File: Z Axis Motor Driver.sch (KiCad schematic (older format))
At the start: 36 parts

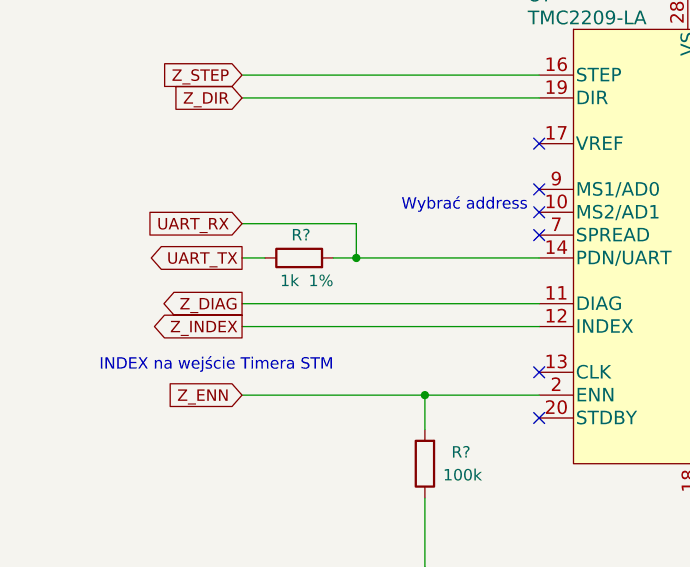
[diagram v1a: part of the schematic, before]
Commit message: Added Polyfuses and replace diodes
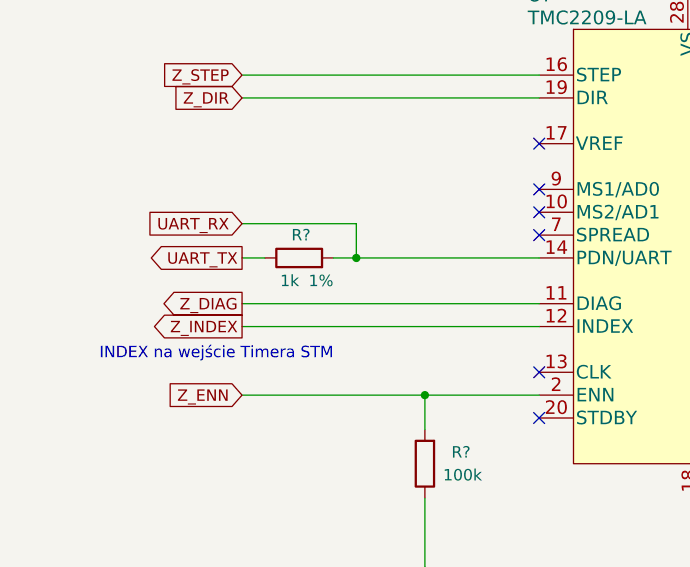
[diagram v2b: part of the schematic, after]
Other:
- note removed: "Wybrać address"
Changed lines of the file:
@@
 $Descr A4 11693 8268
 encoding utf-8
-Sheet 3 9
+Sheet 3 10
 Title "Z Axis Motor Driver"
 Date "2019-12-02"
@@
 Wire Wire Line
 	2700 3850 1400 3850
-Text Notes 1800 4150 2    50   ~ 0
+Text Notes 1800 4100 2    50   ~ 0
 INDEX na wejście Timera STM
 NoConn ~ 2700 4150
@@
 Wire Wire Line
 	2200 4700 2200 5000
-Text Notes 2650 3450 2    50   ~ 0
-Wybrać address
 Text Notes 3700 5550 2    50   ~ 0
 Pin 25 NC można podłączyć do GND jeśli poprawi to rutowanie PCB

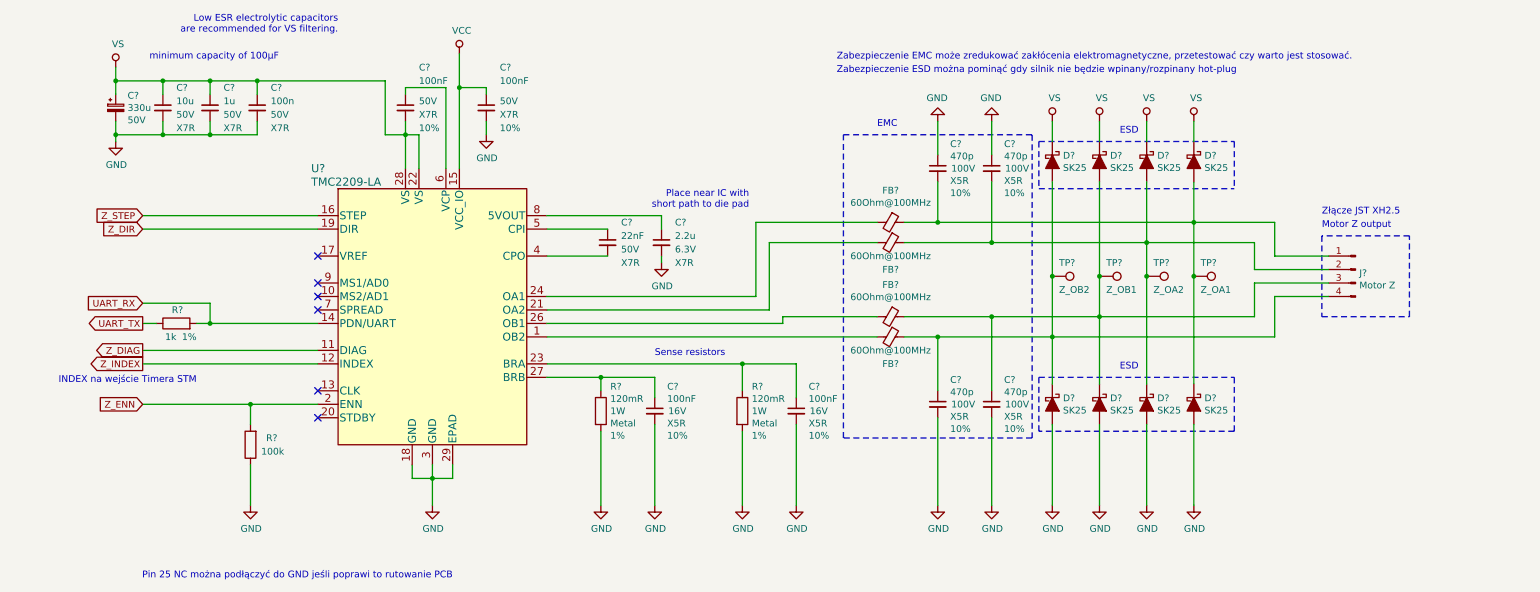
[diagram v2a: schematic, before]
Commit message: Numbering and finishing the schematic
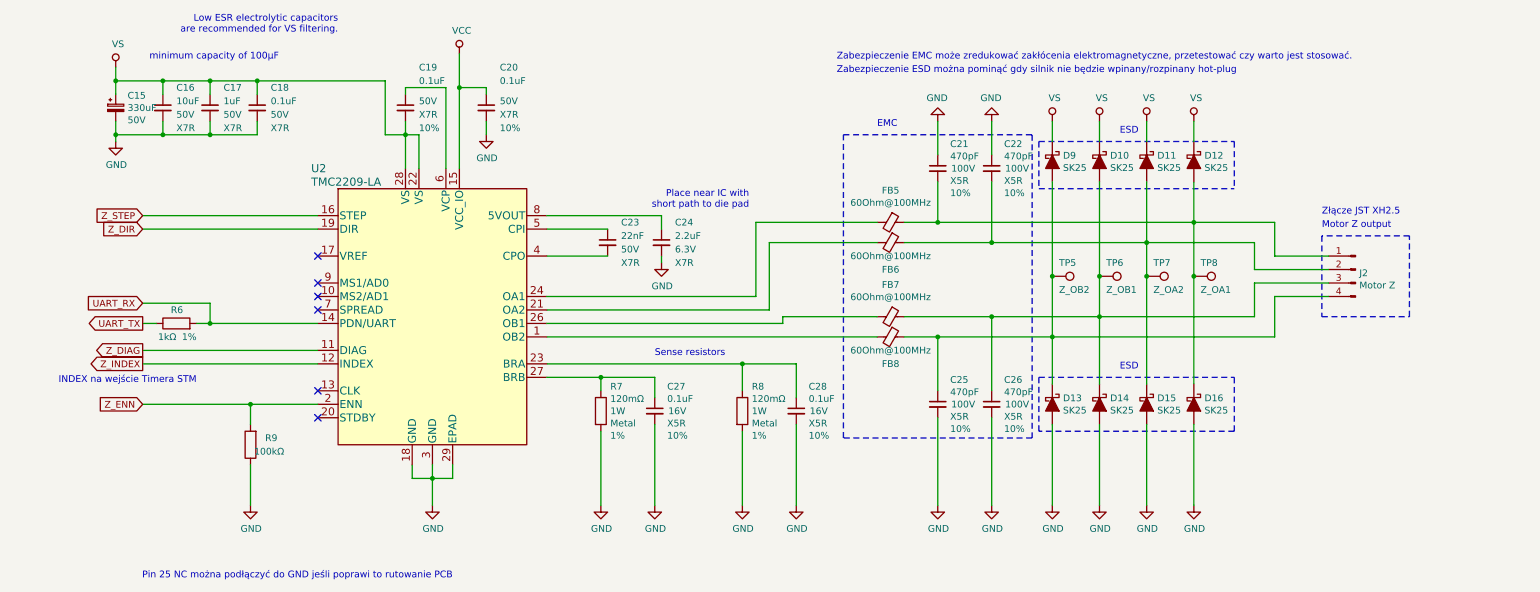
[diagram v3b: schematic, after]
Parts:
- C15: renamed from C?; value 330u -> 330uF
- C16: renamed from C?; value 10u -> 10uF
- C17: renamed from C?; value 1u -> 1uF
- C18: renamed from C?; value 100n -> 0.1uF
- C19, C20, C27, C28: renamed from C?; value 100nF -> 0.1uF
- C21, C22, C25, C26: renamed from C?; value 470p -> 470pF
- C24: renamed from C?; value 2.2u -> 2.2uF
- R6: renamed from R?; value 1k -> 1kΩ
- R7, R8: renamed from R?; value 120mR -> 120mΩ
- R9: renamed from R?; value 100k -> 100kΩ
- gave numbers to parts that had none: 19

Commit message: Shematic almost finished, BOM in KiCad 3/4 finished
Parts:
- C15: footprint (none) -> Capacitor_THT:CP_Radial_D10.0mm_P5.00mm; Cena (none) -> 0.6747; Model (none) -> ED1H331MNN1025; Producent (none) -> Elite; Tolerancja (none) -> 20%; Typ (none) -> THT
- C16: footprint (none) -> Capacitor_SMD:C_1210_3225Metric; Cena (none) -> 1.45250; Model (none) -> CL32B106KBJNNNE; Producent (none) -> SAMSUNG; Tolerancja (none) -> 10%; Typ (none) -> SMD
- C17: footprint (none) -> Capacitor_SMD:C_0805_2012Metric; Cena (none) -> 0.09; Model (none) -> CL21B105KBFNNNE; Producent (none) -> SAMSUNG; Tolerancja (none) -> 10%; Typ (none) -> SMD
- C18: Cena (none) -> 0.05982; Model (none) -> CL10B104KB8NNNC; Producent (none) -> SAMSUNG; Tolerancja (none) -> 10%; Typ (none) -> SMD
- C19, C20: Cena (none) -> 0.05982; Model (none) -> CL10B104KB8NNNC; Producent (none) -> SAMSUNG; Typ (none) -> SMD
- C21: renamed from C23; Cena (none) -> 0.07284; Link (none) -> https://www.tme.eu/pl/details/cc0603krx7r9223/kondensatory-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; Model (none) -> CC0603KRX7R9223; Producent (none) -> YAGEO; Tolerancja (none) -> 10%; Typ (none) -> SMD
- C22: renamed from C27; Cena (none) -> 0.05982; Dielektryk X5R -> X7R; Model (none) -> CL10B104KB8NNNC; Napięcie 16V -> 50V; Producent (none) -> SAMSUNG; Typ (none) -> SMD
- C23: renamed from C24; Cena (none) -> 0.08; Link (none) -> https://www.tme.eu/pl/details/cl10a225kp8nnnc/kondensatory-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; Model (none) -> CL10A225KP8NNNC; Producent (none) -> SAMSUNG; Typ (none) -> SMD
- C24: renamed from C28; Cena (none) -> 0.05982; Dielektryk X5R -> X7R; Model (none) -> CL10B104KB8NNNC; Napięcie 16V -> 50V; Producent (none) -> SAMSUNG; Typ (none) -> SMD
- C25: renamed from C21; footprint Capacitor_SMD:C_0603_1608Metric -> Capacitor_SMD:C_0805_2012Metric; Cena (none) -> 0.09147; Link (none) -> https://www.tme.eu/pl/details/c0805c471j1gac/kondensatory-m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; Model (none) -> C0805C471J1GAC; Producent (none) -> KEMET; Tolerancja 10% -> (none); Typ (none) -> SMD
- C26: renamed from C25; footprint Capacitor_SMD:C_0603_1608Metric -> Capacitor_SMD:C_0805_2012Metric; Cena (none) -> 0.09147; Link (none) -> https://www.tme.eu/pl/details/c0805c471j1gac/kondensatory-m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; Model (none) -> C0805C471J1GAC; Producent (none) -> KEMET; Tolerancja 10% -> (none); Typ (none) -> SMD
- C27: renamed from C22; footprint Capacitor_SMD:C_0603_1608Metric -> Capacitor_SMD:C_0805_2012Metric; Cena (none) -> 0.09147; Link (none) -> https://www.tme.eu/pl/details/c0805c471j1gac/kondensatory-m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; Model (none) -> C0805C471J1GAC; Producent (none) -> KEMET; Tolerancja 10% -> (none); Typ (none) -> SMD
- C28: renamed from C26; footprint Capacitor_SMD:C_0603_1608Metric -> Capacitor_SMD:C_0805_2012Metric; Cena (none) -> 0.09147; Link (none) -> https://www.tme.eu/pl/details/c0805c471j1gac/kondensatory-m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; Model (none) -> C0805C471J1GAC; Producent (none) -> KEMET; Tolerancja 10% -> (none); Typ (none) -> SMD
- D10: renamed from D13; Cena (none) -> 0.2445; Link (none) -> https://www.tme.eu/pl/details/sk25-dio/diody-schottky-smd/d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; Model (none) -> SK25; Opis (none) -> Dioda: prostownicza Schottky; SMD; 50V; 2A; SMB; Producent (none) -> DIOTEC SEMICONDUCTOR; Typ (none) -> SMD
- D11: renamed from D10; Cena (none) -> 0.2445; Link (none) -> https://www.tme.eu/pl/details/sk25-dio/diody-schottky-smd/d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; Model (none) -> SK25; Opis (none) -> Dioda: prostownicza Schottky; SMD; 50V; 2A; SMB; Producent (none) -> DIOTEC SEMICONDUCTOR; Typ (none) -> SMD
- D12: renamed from D14; Cena (none) -> 0.2445; Link (none) -> https://www.tme.eu/pl/details/sk25-dio/diody-schottky-smd/d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; Model (none) -> SK25; Opis (none) -> Dioda: prostownicza Schottky; SMD; 50V; 2A; SMB; Producent (none) -> DIOTEC SEMICONDUCTOR; Typ (none) -> SMD
- D13: renamed from D11; Cena (none) -> 0.2445; Link (none) -> https://www.tme.eu/pl/details/sk25-dio/diody-schottky-smd/d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; Model (none) -> SK25; Opis (none) -> Dioda: prostownicza Schottky; SMD; 50V; 2A; SMB; Producent (none) -> DIOTEC SEMICONDUCTOR; Typ (none) -> SMD
- D14: renamed from D15; Cena (none) -> 0.2445; Link (none) -> https://www.tme.eu/pl/details/sk25-dio/diody-schottky-smd/d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; Model (none) -> SK25; Opis (none) -> Dioda: prostownicza Schottky; SMD; 50V; 2A; SMB; Producent (none) -> DIOTEC SEMICONDUCTOR; Typ (none) -> SMD
- D15: renamed from D12; Cena (none) -> 0.2445; Link (none) -> https://www.tme.eu/pl/details/sk25-dio/diody-schottky-smd/d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; Model (none) -> SK25; Opis (none) -> Dioda: prostownicza Schottky; SMD; 50V; 2A; SMB; Producent (none) -> DIOTEC SEMICONDUCTOR; Typ (none) -> SMD
- D16, D9: Cena (none) -> 0.2445; Link (none) -> https://www.tme.eu/pl/details/sk25-dio/diody-schottky-smd/d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; Model (none) -> SK25; Opis (none) -> Dioda: prostownicza Schottky; SMD; 50V; 2A; SMB; Producent (none) -> DIOTEC SEMICONDUCTOR; Typ (none) -> SMD
- TP5, TP6, TP7, TP8: footprint (none) -> TestPoint:TestPoint_Pad_D1.5mm
- U2: Cena (none) -> 10.30; Link (none) -> https://pl.farnell.com/trinamic/tmc2209-la-t/motor-driver-s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; Model (none) -> TMC2209-LA-T; Opis (none) -> Sterownik/kontroler silnika krokowego, 4.75V do 29V, 2A/1 w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; Producent (none) -> TRINAMIC; Typ (none) -> SMD
- renumbered R9 to R7, R7 to R8, R8 to R9

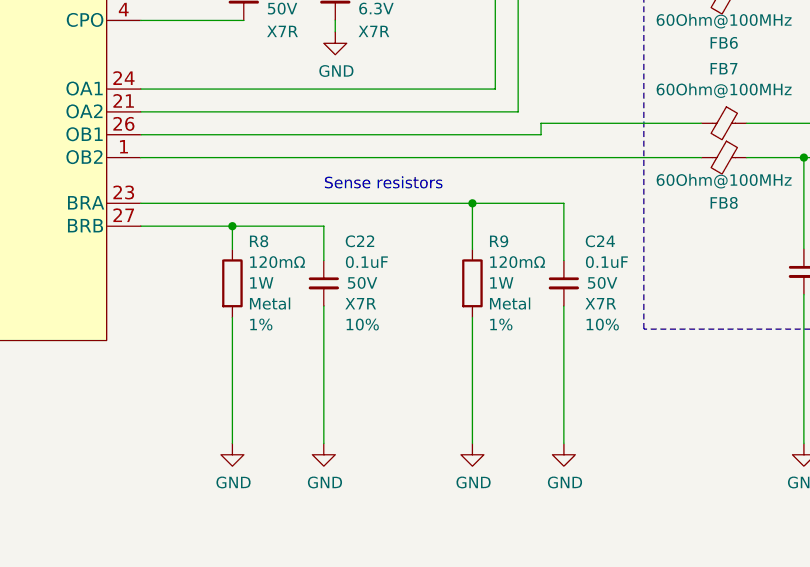
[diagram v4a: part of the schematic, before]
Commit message: BOM in KiCad almost finished, genereated NETLIST, create PCB
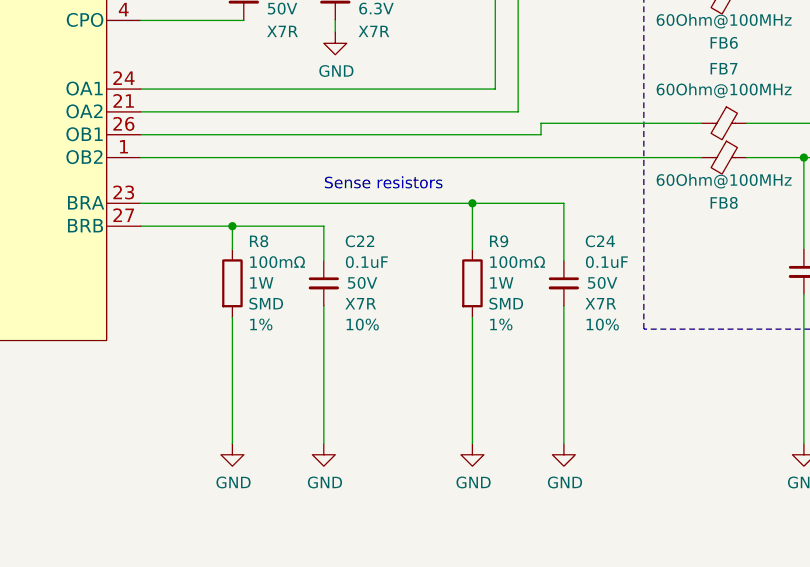
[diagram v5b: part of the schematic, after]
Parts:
- FB5, FB6, FB7, FB8: Cena (none) -> 0.13674; Link (none) -> https://www.tme.eu/pl/details/blm21pg600sn1d/ferryty-korali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; Opis (none) -> Ferryt: koralik; Imp.@ 100MHz: 60Ω; Montaż: SMD; 3A; Obud: 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; Producent (none) -> MURATA; Typ (none) -> SMD
- J2: Cena (none) -> 0.81567; Link (none) -> https://www.tme.eu/pl/details/b4b-xh-a/zlacza-sygnalowe-ras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; Model (none) -> B4B-XH-A; Opis (none) -> Gniazdo; przewód-płytka; męskie; XH; 2,5mm; PIN: 4; THT; 25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; Producent (none) -> JST; Typ (none) -> THT
- R6: Cena (none) -> 0.04651; Link (none) -> https://www.tme.eu/pl/details/smd0603-1k-1%25/rezystory-smd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; Model (none) -> 0603SAF1001T5E; Opis (none) -> Rezystor: thick film; SMD; 0603; 1kΩ; 0,1W; ±1%; -55÷155°C; Producent (none) -> ROYAL OHM; Typ (none) -> SMD
- R7: Cena (none) -> 0.04651; Typ (none) -> SMD
- R8, R9: value 120mΩ -> 100mΩ; Cena (none) -> 0.76246; Link (none) -> https://www.tme.eu/pl/details/cs2010-0r1-1%25-hp/rezystory-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; Model (none) -> CS10FTFTR100; Opis (none) -> Rezystor: thick film; pomiarowy; SMD; 2010; 100mΩ; 1W; ±1%; Producent (none) -> VIKING; Typ Metal -> SMD
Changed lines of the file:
@@
 P 4800 4300
 F 0 "R8" H 4870 4482 50  0000 L CNN
-F 1 "120mΩ" H 4870 4391 50  0000 L CNN
+F 1 "100mΩ" H 4870 4391 50  0000 L CNN
 F 2 "Resistor_SMD:R_2010_5025Metric" V 4730 4300 50  0001 C CNN
 F 3 "~" H 4800 4300 50  0001 C CNN
 F 4 "1W" H 4870 4300 50  0000 L CNN "Moc"
-F 5 "Metal" H 4870 4209 50  0000 L CNN "Typ"
+F 5 "SMD" H 4870 4209 50  0000 L CNN "Typ"
 F 6 "1%" H 4870 4118 50  0000 L CNN "Tolerancja"
-F 7 "" H 4800 4300 50  0001 C CNN "Model"
+F 7 "CS10FTFTR100" H 4800 4300 50  0001 C CNN "Model"
+F 8 "0.76246" H 4800 4300 50  0001 C CNN "Cena"
+F 9 "https://www.tme.eu/pl/details/cs2010-0r1-1%25-hp/rezystory-smd-2010/viking/cs10ftftr100/" H 4800 4300 50  0001 C CNN "Link"
+F 10 "Rezystor: thick film; pomiarowy; SMD; 2010; 100mΩ; 1W; ±1%" H 4800 4300 50  0001 C CNN "Opis"
+F 11 "VIKING" H 4800 4300 50  0001 C CNN "Producent"
 	1    4800 4300
 	1    0    0    -1
@@
 P 5850 4300
 F 0 "R9" H 5920 4482 50  0000 L CNN
-F 1 "120mΩ" H 5920 4391 50  0000 L CNN
+F 1 "100mΩ" H 5920 4391 50  0000 L CNN
 F 2 "Resistor_SMD:R_2010_5025Metric" V 5780 4300 50  0001 C CNN
 F 3 "~" H 5850 4300 50  0001 C CNN
 F 4 "1W" H 5920 4300 50  0000 L CNN "Moc"
-F 5 "Metal" H 5920 4209 50  0000 L CNN "Typ"
+F 5 "SMD" H 5920 4209 50  0000 L CNN "Typ"
 F 6 "1%" H 5920 4118 50  0000 L CNN "Tolerancja"
-F 7 "" H 5850 4300 50  0001 C CNN "Model"
+F 7 "CS10FTFTR100" H 5850 4300 50  0001 C CNN "Model"
+F 8 "0.76246" H 5850 4300 50  0001 C CNN "Cena"
+F 9 "https://www.tme.eu/pl/details/cs2010-0r1-1%25-hp/rezystory-smd-2010/viking/cs10ftftr100/" H 5850 4300 50  0001 C CNN "Link"
+F 10 "Rezystor: thick film; pomiarowy; SMD; 2010; 100mΩ; 1W; ±1%" H 5850 4300 50  0001 C CNN "Opis"
+F 11 "VIKING" H 5850 4300 50  0001 C CNN "Producent"
 	1    5850 4300
 	1    0    0    -1
@@
 F 3 "~" H 6950 2900 50  0001 C CNN
 F 4 "BLM21PG600SN1D" V 6950 2900 50  0001 C CNN "Model"
+F 5 "0.13674" H 6950 2900 50  0001 C CNN "Cena"
+F 6 "https://www.tme.eu/pl/details/blm21pg600sn1d/ferryty-koraliki/murata/" H 6950 2900 50  0001 C CNN "Link"
+F 7 "Ferryt: koralik; Imp.@ 100MHz: 60Ω; Montaż: SMD; 3A; Obud: 0805" H 6950 2900 50  0001 C CNN "Opis"
+F 8 "MURATA" H 6950 2900 50  0001 C CNN "Producent"
+F 9 "SMD" H 6950 2900 50  0001 C CNN "Typ"
 	1    6950 2900
 	0    1    1    0
@@
 F 3 "~" H 6950 3050 50  0001 C CNN
 F 4 "BLM21PG600SN1D" V 6950 3050 50  0001 C CNN "Model"
+F 5 "0.13674" H 6950 3050 50  0001 C CNN "Cena"
+F 6 "https://www.tme.eu/pl/details/blm21pg600sn1d/ferryty-koraliki/murata/" H 6950 3050 50  0001 C CNN "Link"
+F 7 "Ferryt: koralik; Imp.@ 100MHz: 60Ω; Montaż: SMD; 3A; Obud: 0805" H 6950 3050 50  0001 C CNN "Opis"
+F 8 "MURATA" H 6950 3050 50  0001 C CNN "Producent"
+F 9 "SMD" H 6950 3050 50  0001 C CNN "Typ"
 	1    6950 3050
 	0    1    1    0
@@
 F 3 "~" H 6950 3600 50  0001 C CNN
 F 4 "BLM21PG600SN1D" V 6950 3600 50  0001 C CNN "Model"
+F 5 "0.13674" H 6950 3600 50  0001 C CNN "Cena"
+F 6 "https://www.tme.eu/pl/details/blm21pg600sn1d/ferryty-koraliki/murata/" H 6950 3600 50  0001 C CNN "Link"
+F 7 "Ferryt: koralik; Imp.@ 100MHz: 60Ω; Montaż: SMD; 3A; Obud: 0805" H 6950 3600 50  0001 C CNN "Opis"
+F 8 "MURATA" H 6950 3600 50  0001 C CNN "Producent"
+F 9 "SMD" H 6950 3600 50  0001 C CNN "Typ"
 	1    6950 3600
 	0    1    1    0
@@
 F 3 "~" H 6950 3750 50  0001 C CNN
 F 4 "BLM21PG600SN1D" V 6950 3750 50  0001 C CNN "Model"
+F 5 "0.13674" H 6950 3750 50  0001 C CNN "Cena"
+F 6 "https://www.tme.eu/pl/details/blm21pg600sn1d/ferryty-koraliki/murata/" H 6950 3750 50  0001 C CNN "Link"
+F 7 "Ferryt: koralik; Imp.@ 100MHz: 60Ω; Montaż: SMD; 3A; Obud: 0805" H 6950 3750 50  0001 C CNN "Opis"
+F 8 "MURATA" H 6950 3750 50  0001 C CNN "Producent"
+F 9 "SMD" H 6950 3750 50  0001 C CNN "Typ"
 	1    6950 3750
 	0    1    1    0
@@
 F 2 "Connector_JST:JST_XH_B4B-XH-AM_1x04_P2.50mm_Vertical" H 10400 3250 50  0001 C CNN
 F 3 "~" H 10400 3250 50  0001 C CNN
+F 4 "0.81567" H 10400 3250 50  0001 C CNN "Cena"
+F 5 "https://www.tme.eu/pl/details/b4b-xh-a/zlacza-sygnalowe-raster-2-50mm/jst/" H 10400 3250 50  0001 C CNN "Link"
+F 6 "B4B-XH-A" H 10400 3250 50  0001 C CNN "Model"
+F 7 "Gniazdo; przewód-płytka; męskie; XH; 2,5mm; PIN: 4; THT; 250V; 3A" H 10400 3250 50  0001 C CNN "Opis"
+F 8 "JST" H 10400 3250 50  0001 C CNN "Producent"
+F 9 "THT" H 10400 3250 50  0001 C CNN "Typ"
 	1    10400 3250
 	-1   0    0    -1
@@
 F 3 "~" H 1650 3650 50  0001 C CNN
 F 4 "1%" V 1550 3500 50  0000 L CNN "Tolerancja"
-F 5 "" H 1650 3650 50  0001 C CNN "Model"
+F 5 "0603SAF1001T5E" H 1650 3650 50  0001 C CNN "Model"
+F 6 "0.04651" H 1650 3650 50  0001 C CNN "Cena"
+F 7 "https://www.tme.eu/pl/details/smd0603-1k-1%25/rezystory-smd-0603/royal-ohm/0603saf1001t5e/" H 1650 3650 50  0001 C CNN "Link"
+F 8 "Rezystor: thick film; SMD; 0603; 1kΩ; 0,1W; ±1%; -55÷155°C" H 1650 3650 50  0001 C CNN "Opis"
+F 9 "ROYAL OHM" H 1650 3650 50  0001 C CNN "Producent"
+F 10 "SMD" H 1650 3650 50  0001 C CNN "Typ"
 	1    1650 3650
 	0    -1   -1   0
@@
 F 3 "~" H 2200 4550 50  0001 C CNN
 F 4 "" H 2200 4550 50  0001 C CNN "Model"
+F 5 "0.04651" H 2200 4550 50  0001 C CNN "Cena"
+F 6 "SMD" H 2200 4550 50  0001 C CNN "Typ"
 	1    2200 4550
 	-1   0    0    1
